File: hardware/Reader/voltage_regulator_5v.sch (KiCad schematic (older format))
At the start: 5 parts

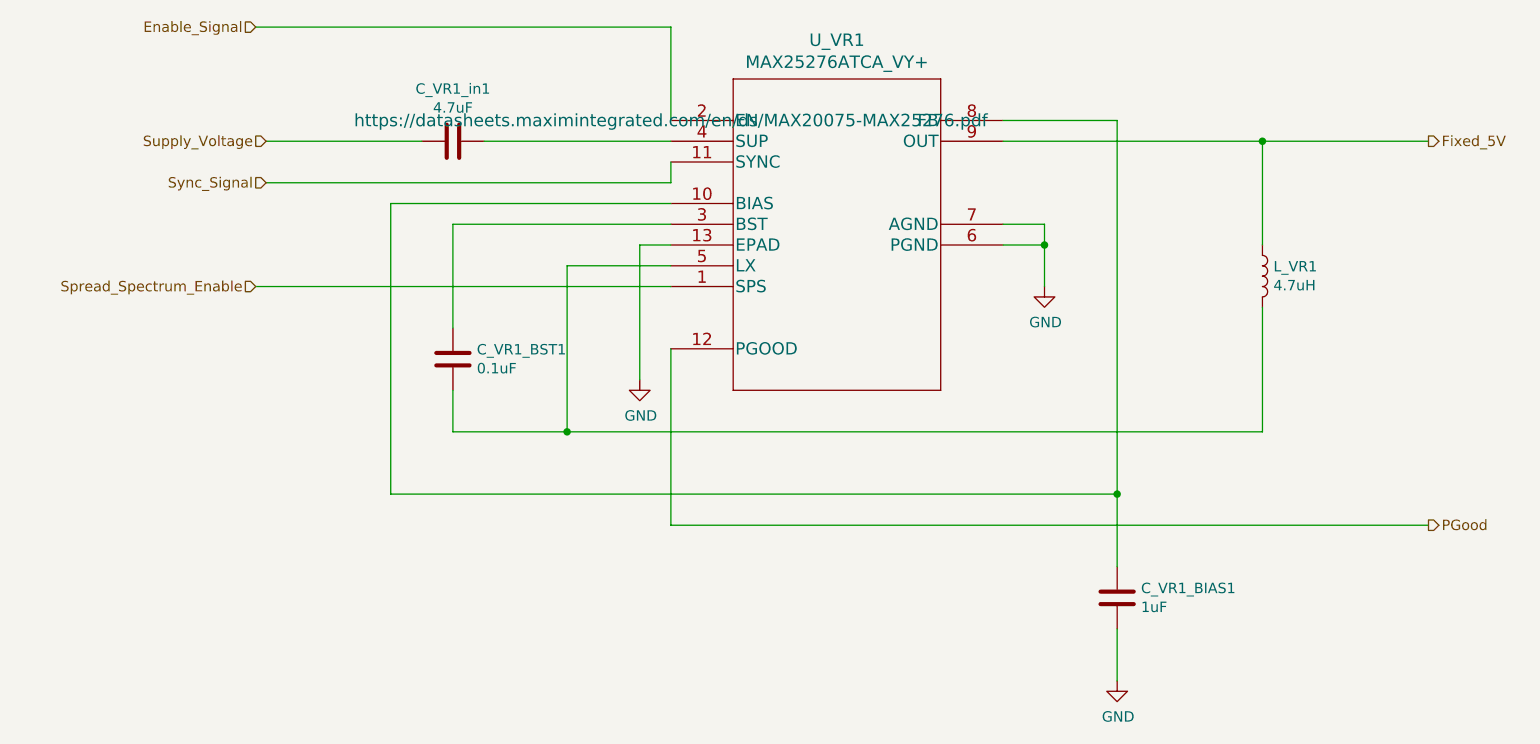
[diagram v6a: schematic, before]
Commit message: Fixed bugs in schematic. Updated BOM list. Swapped to using ESP32 holder. Updated PCB layout to v0.0.2. Updated schematic to v0.0.4
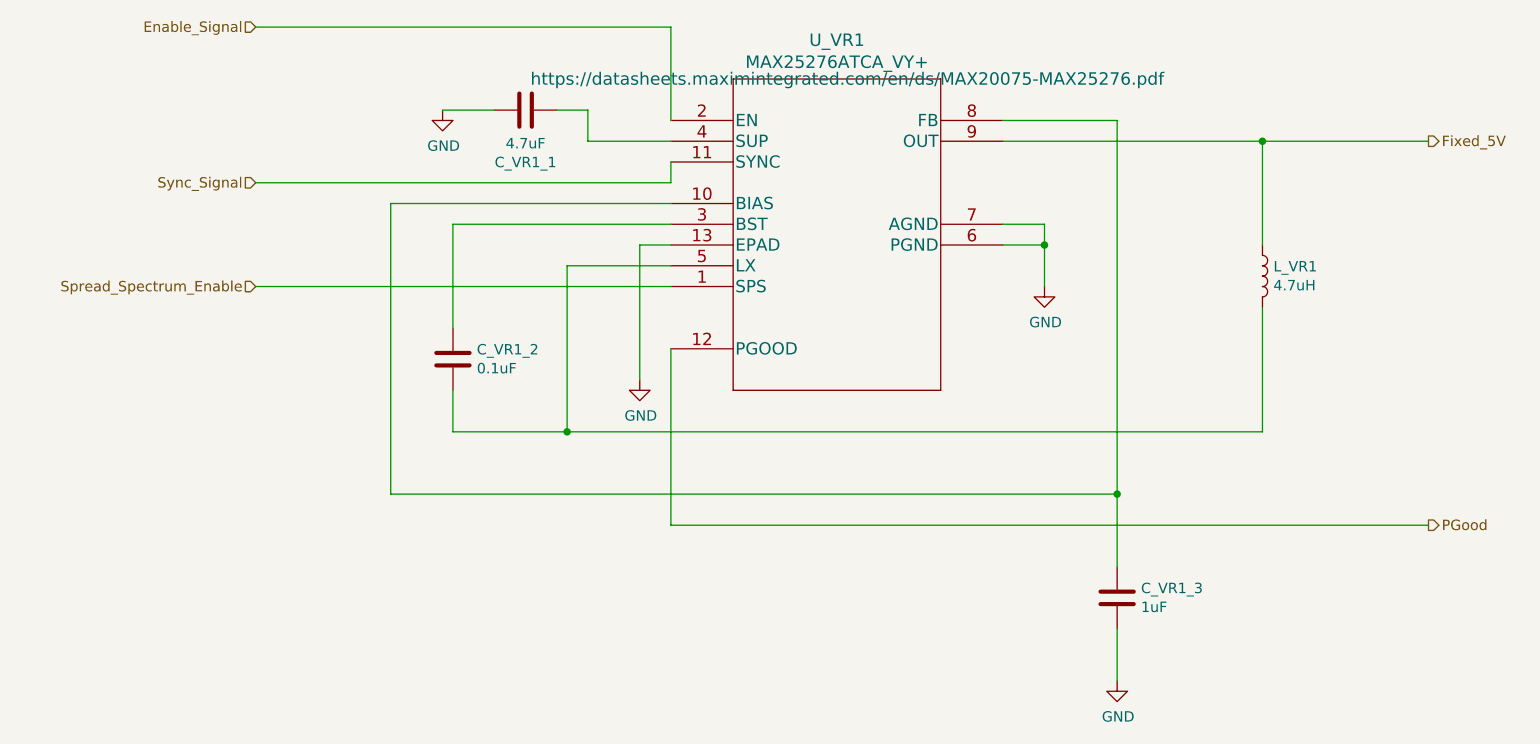
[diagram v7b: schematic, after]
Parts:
- renumbered C_VR1_in1 to C_VR1_1, C_VR1_BST1 to C_VR1_2, C_VR1_BIAS1 to C_VR1_3
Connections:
- net Supply_Voltage is gone; now on an unnamed net: C_VR1_1.2
- net GND: now also C_VR1_1.1
- net at U_VR1.4 (SUP): no longer C_VR1_1.1
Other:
- moved on the sheet: C_VR1_1
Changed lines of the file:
@@
 Sheet 18 19
 Title "CANnect Reader | Voltage Regulator (5V)"
-Date "2020-10-27"
-Rev "0.0.03"
+Date "2020-10-28"
+Rev "0.0.04"
 Comp "CANtech"
 Comment1 "Created by Choong Jin Ng | jin8383@gmail.com"
@@
 F 1 "MAX25276ATCA_VY+" H 4600 2481 60  0000 C CNN
 F 2 "footprints:MAX25276ATCA&slash_VY&plus_" H 4600 2440 60  0001 C CNN
-F 3 "https://datasheets.maximintegrated.com/en/ds/MAX20075-MAX25276.pdf" H 3800 2200 60  0000 C CNN
+F 3 "https://datasheets.maximintegrated.com/en/ds/MAX20075-MAX25276.pdf" H 4650 2400 60  0000 C CNN
 F 4 "MAX25276ATCA/VY+" H 3800 2200 50  0001 C CNN "Part Name"
 F 5 "Maxim Integrated" H 3800 2200 50  0001 C CNN "Manufacturer"
@@
 Text HLabel 1800 1750 0    50   Input ~ 0
 Enable_Signal
-Text HLabel 1850 2300 0    50   Input ~ 0
-Supply_Voltage
-Text HLabel 1850 2500 0    50   Input ~ 0
+Text HLabel 1800 2500 0    50   Input ~ 0
 Sync_Signal
 Text HLabel 7450 2300 2    50   Output ~ 0
@@
 	5950 4650 5950 4900
 $Comp
-L Device:C C_VR1_in1
+L Device:C C_VR1_1
 U 1 1 5F9F0C9F
-P 2750 2300
-F 0 "C_VR1_in1" V 2498 2300 50  0000 C CNN
-F 1 "4.7uF" V 2589 2300 50  0000 C CNN
-F 2 "footprints:C1206C475K3RACAUTO" H 2788 2150 50  0001 C CNN
-F 3 "https://api.kemet.com/component-edge/download/specsheet/C1206C475K3RACAUTO.pdf" H 2750 2300 50  0001 C CNN
-F 4 "C1206C475K3RACAUTO" H 2750 2300 50  0001 C CNN "Part Name"
-F 5 "Kermet" H 2750 2300 50  0001 C CNN "Manufacturer"
-F 6 "DigiKey Canada" H 2750 2300 50  0001 C CNN "Vendor"
-F 7 "399-7029-1-ND" H 2750 2300 50  0001 C CNN "digikeypn"
-	1    2750 2300
-	0    1    1    0
+P 3100 2150
+F 0 "C_VR1_1" V 2848 2150 50  0000 C CNN
+F 1 "4.7uF" V 2939 2150 50  0000 C CNN
+F 2 "footprints:C1206C475K3RACAUTO" H 3138 2000 50  0001 C CNN
+F 3 "https://api.kemet.com/component-edge/download/specsheet/C1206C475K3RACAUTO.pdf" H 3100 2150 50  0001 C CNN
+F 4 "C1206C475K3RACAUTO" H 3100 2150 50  0001 C CNN "Part Name"
+F 5 "Kermet" H 3100 2150 50  0001 C CNN "Manufacturer"
+F 6 "DigiKey Canada" H 3100 2150 50  0001 C CNN "Vendor"
+F 7 "399-7029-1-ND" H 3100 2150 50  0001 C CNN "digikeypn"
+	1    3100 2150
+	0    -1   -1   0
 $EndComp
 Wire Wire Line
@@
 	3800 1750 3800 2200
 Wire Wire Line
-	1850 2300 2600 2300
-Wire Wire Line
-	2900 2300 3800 2300
-Wire Wire Line
-	1850 2500 3800 2500
+	1800 2500 3800 2500
 Wire Wire Line
 	3800 2500 3800 2400
@@
 	6650 2300 7450 2300
 $Comp
-L Device:C C_VR1_BST1
+L Device:C C_VR1_2
 U 1 1 5F9F38FF
 P 2750 3350
-F 0 "C_VR1_BST1" H 2865 3396 50  0000 L CNN
+F 0 "C_VR1_2" H 2865 3396 50  0000 L CNN
 F 1 "0.1uF" H 2865 3305 50  0000 L CNN
 F 2 "footprints:CAPC1608X90" H 2788 3200 50  0001 C CNN
@@
 	1800 3000 3800 3000
 $Comp
-L Device:C C_VR1_BIAS1
+L Device:C C_VR1_3
 U 1 1 5F9EFBD6
 P 5950 4500
-F 0 "C_VR1_BIAS1" H 6065 4546 50  0000 L CNN
+F 0 "C_VR1_3" H 6065 4546 50  0000 L CNN
 F 1 "1uF" H 6065 4455 50  0000 L CNN
 F 2 "footprints:0603" H 5988 4350 50  0001 C CNN
@@
 Wire Wire Line
 	5950 4000 5950 4350
+Wire Wire Line
+	3800 2300 3400 2300
+Wire Wire Line
+	3400 2300 3400 2150
+Wire Wire Line
+	3400 2150 3250 2150
+$Comp
+L power:GND #PWR0107
+U 1 1 5F994A83
+P 2700 2150
+F 0 "#PWR0107" H 2700 1900 50  0001 C CNN
+F 1 "GND" H 2705 1977 50  0000 C CNN
+F 2 "" H 2700 2150 50  0001 C CNN
+F 3 "" H 2700 2150 50  0001 C CNN
+	1    2700 2150
+	1    0    0    -1
+$EndComp
+Wire Wire Line
+	2700 2150 2950 2150
 $EndSCHEMATC
